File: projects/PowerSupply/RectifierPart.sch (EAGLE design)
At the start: 12 parts, among them X1 IN, X2 PRI, X3 SEC, X4 OUT

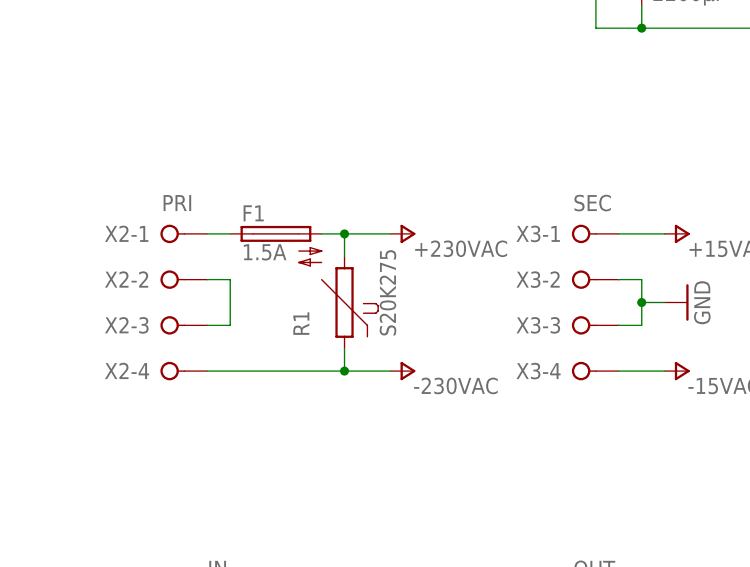
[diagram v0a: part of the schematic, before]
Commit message: fix(rect): replaced s20k275 with s20k230
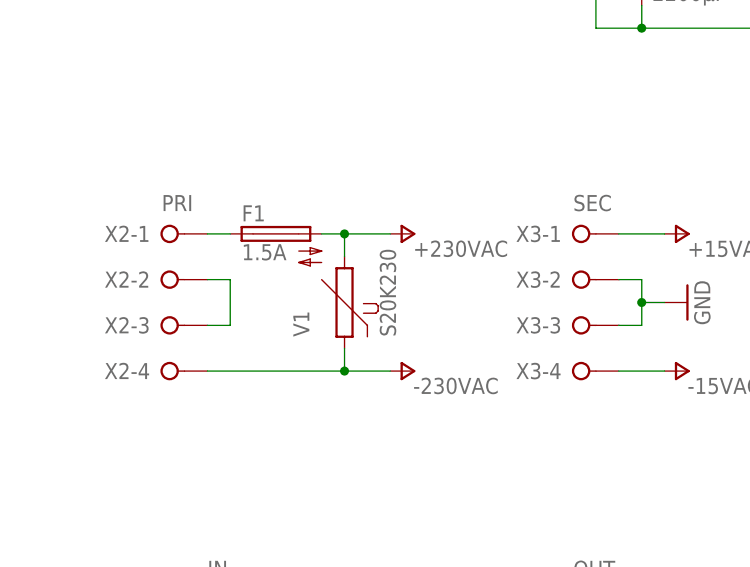
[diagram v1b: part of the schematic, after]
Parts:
- removed R1: S20K275, varistor:S20K275
- added V1: S20K230, varistor:S20K230
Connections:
- net +230VAC: now also V1.2; no longer R1.2
- net -230VAC: now also V1.1; no longer R1.1
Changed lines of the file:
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@@
 <grid distance="0.1" unitdist="inch" unit="inch" style="lines" multiple="1" display="no" altdistance="0.01" altunitdist="inch" altunit="inch"/>
 <layers>
-<layer number="1" name="Top" color="4" fill="1" visible="no" active="no"/>
-<layer number="16" name="Bottom" color="1" fill="1" visible="no" active="no"/>
-<layer number="17" name="Pads" color="2" fill="1" visible="no" active="no"/>
-<layer number="18" name="Vias" color="2" fill="1" visible="no" active="no"/>
-<layer number="19" name="Unrouted" color="6" fill="1" visible="no" active="no"/>
-<layer number="20" name="Dimension" color="24" fill="1" visible="no" active="no"/>
-<layer number="21" name="tPlace" color="7" fill="1" visible="no" active="no"/>
-<layer number="22" name="bPlace" color="7" fill="1" visible="no" active="no"/>
-<layer number="23" name="tOrigins" color="15" fill="1" visible="no" active="no"/>
-<layer number="24" name="bOrigins" color="15" fill="1" visible="no" active="no"/>
-<layer number="25" name="tNames" color="7" fill="1" visible="no" active="no"/>
-<layer number="26" name="bNames" color="7" fill="1" visible="no" active="no"/>
-<layer number="27" name="tValues" color="7" fill="1" visible="no" active="no"/>
-<layer number="28" name="bValues" color="7" fill="1" visible="no" active="no"/>
+<layer number="1" name="Top" color="4" fill="1" visible="yes" active="no"/>
+<layer number="16" name="Bottom" color="1" fill="1" visible="yes" active="no"/>
+<layer number="17" name="Pads" color="2" fill="1" visible="yes" active="no"/>
+<layer number="18" name="Vias" color="2" fill="1" visible="yes" active="no"/>
+<layer number="19" name="Unrouted" color="6" fill="1" visible="yes" active="no"/>
+<layer number="20" name="Dimension" color="24" fill="1" visible="yes" active="no"/>
+<layer number="21" name="tPlace" color="7" fill="1" visible="yes" active="no"/>
+<layer number="22" name="bPlace" color="7" fill="1" visible="yes" active="no"/>
+<layer number="23" name="tOrigins" color="15" fill="1" visible="yes" active="no"/>
+<layer number="24" name="bOrigins" color="15" fill="1" visible="yes" active="no"/>
+<layer number="25" name="tNames" color="7" fill="1" visible="yes" active="no"/>
+<layer number="26" name="bNames" color="7" fill="1" visible="yes" active="no"/>
+<layer number="27" name="tValues" color="7" fill="1" visible="yes" active="no"/>
+<layer number="28" name="bValues" color="7" fill="1" visible="yes" active="no"/>
 <layer number="29" name="tStop" color="7" fill="3" visible="no" active="no"/>
 <layer number="30" name="bStop" color="7" fill="6" visible="no" active="no"/>
@@
 <layer number="35" name="tGlue" color="7" fill="4" visible="no" active="no"/>
 <layer number="36" name="bGlue" color="7" fill="5" visible="no" active="no"/>
-<layer number="37" name="tTest" color="7" fill="1" visible="no" active="no"/>
-<layer number="38" name="bTest" color="7" fill="1" visible="no" active="no"/>
+<layer number="37" name="tTest" color="7" fill="1" visible="yes" active="no"/>
+<layer number="38" name="bTest" color="7" fill="1" visible="yes" active="no"/>
 <layer number="39" name="tKeepout" color="4" fill="11" visible="no" active="no"/>
 <layer number="40" name="bKeepout" color="1" fill="11" visible="no" active="no"/>
@@
 <layer number="44" name="Drills" color="7" fill="1" visible="no" active="no"/>
 <layer number="45" name="Holes" color="7" fill="1" visible="no" active="no"/>
-<layer number="46" name="Milling" color="3" fill="1" visible="no" active="no"/>
-<layer number="47" name="Measures" color="7" fill="1" visible="no" active="no"/>
-<layer number="48" name="Document" color="7" fill="1" visible="no" active="no"/>
-<layer number="49" name="Reference" color="7" fill="1" visible="no" active="no"/>
-<layer number="51" name="tDocu" color="7" fill="1" visible="no" active="no"/>
-<layer number="52" name="bDocu" color="7" fill="1" visible="no" active="no"/>
+<layer number="46" name="Milling" color="3" fill="1" visible="yes" active="no"/>
+<layer number="47" name="Measures" color="7" fill="1" visible="yes" active="no"/>
+<layer number="48" name="Document" color="7" fill="1" visible="yes" active="no"/>
+<layer number="49" name="Reference" color="7" fill="1" visible="yes" active="no"/>
+<layer number="51" name="tDocu" color="7" fill="1" visible="yes" active="no"/>
+<layer number="52" name="bDocu" color="7" fill="1" visible="yes" active="no"/>
 <layer number="88" name="SimResults" color="9" fill="1" visible="yes" active="yes"/>
 <layer number="89" name="SimProbes" color="9" fill="1" visible="yes" active="yes"/>
@@
 <part name="C4" library="rcl" library_urn="urn:adsk.eagle:library:334" deviceset="CPOL-EU" device="E7.5-16" package3d_urn="urn:adsk.eagle:package:23382/2" value="2200µF"/>
 <part name="FRAME1" library="frames" library_urn="urn:adsk.eagle:library:229" deviceset="A4L-LOC" device=""/>
-<part name="R1" library="varistor" library_urn="urn:adsk.eagle:library:410" deviceset="S20K275" device="" package3d_urn="urn:adsk.eagle:package:30604/1"/>
+<part name="V1" library="varistor" library_urn="urn:adsk.eagle:library:410" deviceset="S20K230" device="" package3d_urn="urn:adsk.eagle:package:30579/1"/>
 <part name="F1" library="fuse" library_urn="urn:adsk.eagle:library:233" deviceset="SH22,5A" device="" package3d_urn="urn:adsk.eagle:package:14070/1" value="1.5A"/>
 <part name="F2" library="fuse" library_urn="urn:adsk.eagle:library:233" deviceset="SH22,5A" device="" package3d_urn="urn:adsk.eagle:package:14070/1" value="10A"/>
@@
 <attribute name="SHEET" x="230.505" y="5.08" size="2.54" layer="94"/>
 </instance>
-<instance part="R1" gate="G$1" x="45.72" y="109.22" smashed="yes" rot="R90">
+<instance part="V1" gate="G$1" x="45.72" y="109.22" smashed="yes" rot="R90">
 <attribute name="NAME" x="41.8084" y="105.41" size="1.778" layer="95" rot="R90"/>
 <attribute name="VALUE" x="51.435" y="105.41" size="1.778" layer="96" rot="R90"/>
@@
 <pinref part="F1" gate="1" pin="2"/>
 <wire x1="43.18" y1="116.84" x2="45.72" y2="116.84" width="0.1524" layer="91"/>
-<pinref part="R1" gate="G$1" pin="2"/>
+<pinref part="V1" gate="G$1" pin="2"/>
 <wire x1="45.72" y1="116.84" x2="50.8" y2="116.84" width="0.1524" layer="91"/>
 <wire x1="45.72" y1="114.3" x2="45.72" y2="116.84" width="0.1524" layer="91"/>
@@
 <pinref part="X2" gate="-4" pin="KL"/>
 <wire x1="50.8" y1="101.6" x2="45.72" y2="101.6" width="0.1524" layer="91"/>
-<pinref part="R1" gate="G$1" pin="1"/>
+<pinref part="V1" gate="G$1" pin="1"/>
 <wire x1="45.72" y1="101.6" x2="30.48" y2="101.6" width="0.1524" layer="91"/>
 <wire x1="45.72" y1="104.14" x2="45.72" y2="101.6" width="0.1524" layer="91"/>

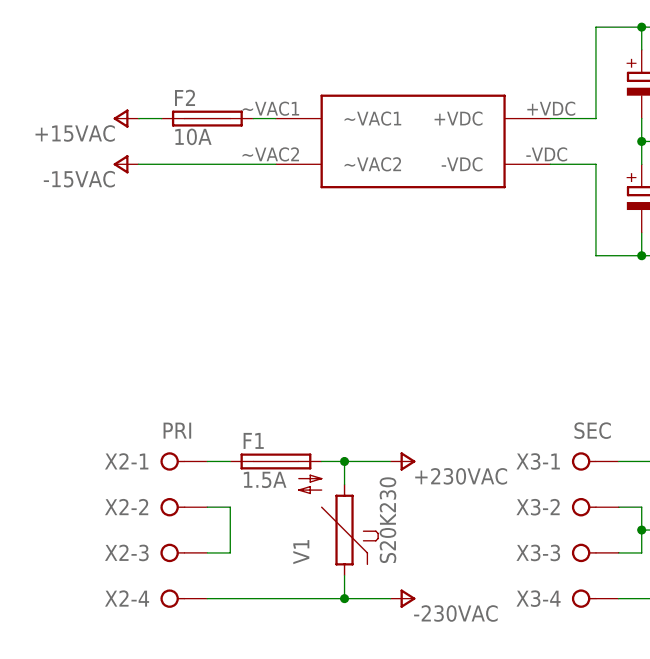
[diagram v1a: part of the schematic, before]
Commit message: feat: rectifier fuse values modified
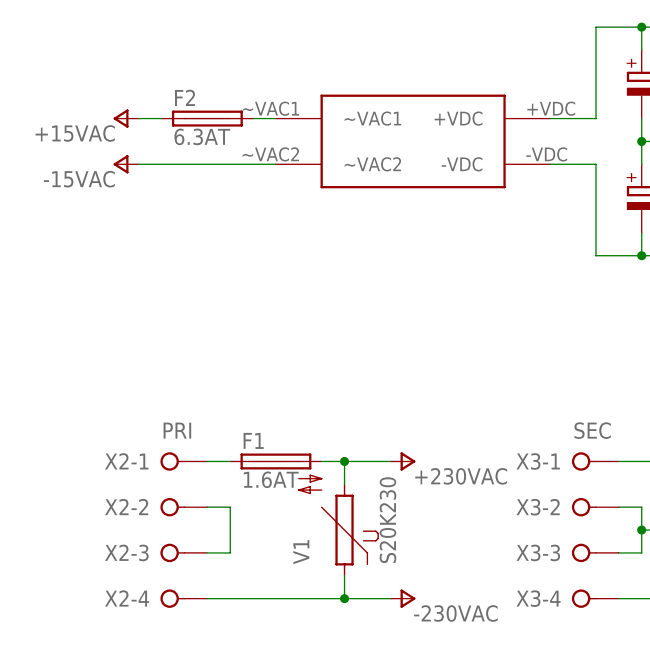
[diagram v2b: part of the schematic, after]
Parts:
- F1: value 1.5A -> 1.6AT
- F2: value 10A -> 6.3AT
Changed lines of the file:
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@@
 <grid distance="0.1" unitdist="inch" unit="inch" style="lines" multiple="1" display="no" altdistance="0.01" altunitdist="inch" altunit="inch"/>
 <layers>
-<layer number="1" name="Top" color="4" fill="1" visible="yes" active="no"/>
-<layer number="16" name="Bottom" color="1" fill="1" visible="yes" active="no"/>
-<layer number="17" name="Pads" color="2" fill="1" visible="yes" active="no"/>
-<layer number="18" name="Vias" color="2" fill="1" visible="yes" active="no"/>
-<layer number="19" name="Unrouted" color="6" fill="1" visible="yes" active="no"/>
-<layer number="20" name="Dimension" color="24" fill="1" visible="yes" active="no"/>
-<layer number="21" name="tPlace" color="7" fill="1" visible="yes" active="no"/>
-<layer number="22" name="bPlace" color="7" fill="1" visible="yes" active="no"/>
-<layer number="23" name="tOrigins" color="15" fill="1" visible="yes" active="no"/>
-<layer number="24" name="bOrigins" color="15" fill="1" visible="yes" active="no"/>
-<layer number="25" name="tNames" color="7" fill="1" visible="yes" active="no"/>
-<layer number="26" name="bNames" color="7" fill="1" visible="yes" active="no"/>
-<layer number="27" name="tValues" color="7" fill="1" visible="yes" active="no"/>
-<layer number="28" name="bValues" color="7" fill="1" visible="yes" active="no"/>
+<layer number="1" name="Top" color="4" fill="1" visible="no" active="no"/>
+<layer number="16" name="Bottom" color="1" fill="1" visible="no" active="no"/>
+<layer number="17" name="Pads" color="2" fill="1" visible="no" active="no"/>
+<layer number="18" name="Vias" color="2" fill="1" visible="no" active="no"/>
+<layer number="19" name="Unrouted" color="6" fill="1" visible="no" active="no"/>
+<layer number="20" name="Dimension" color="24" fill="1" visible="no" active="no"/>
+<layer number="21" name="tPlace" color="7" fill="1" visible="no" active="no"/>
+<layer number="22" name="bPlace" color="7" fill="1" visible="no" active="no"/>
+<layer number="23" name="tOrigins" color="15" fill="1" visible="no" active="no"/>
+<layer number="24" name="bOrigins" color="15" fill="1" visible="no" active="no"/>
+<layer number="25" name="tNames" color="7" fill="1" visible="no" active="no"/>
+<layer number="26" name="bNames" color="7" fill="1" visible="no" active="no"/>
+<layer number="27" name="tValues" color="7" fill="1" visible="no" active="no"/>
+<layer number="28" name="bValues" color="7" fill="1" visible="no" active="no"/>
 <layer number="29" name="tStop" color="7" fill="3" visible="no" active="no"/>
 <layer number="30" name="bStop" color="7" fill="6" visible="no" active="no"/>
@@
 <layer number="35" name="tGlue" color="7" fill="4" visible="no" active="no"/>
 <layer number="36" name="bGlue" color="7" fill="5" visible="no" active="no"/>
-<layer number="37" name="tTest" color="7" fill="1" visible="yes" active="no"/>
-<layer number="38" name="bTest" color="7" fill="1" visible="yes" active="no"/>
+<layer number="37" name="tTest" color="7" fill="1" visible="no" active="no"/>
+<layer number="38" name="bTest" color="7" fill="1" visible="no" active="no"/>
 <layer number="39" name="tKeepout" color="4" fill="11" visible="no" active="no"/>
 <layer number="40" name="bKeepout" color="1" fill="11" visible="no" active="no"/>
@@
 <layer number="44" name="Drills" color="7" fill="1" visible="no" active="no"/>
 <layer number="45" name="Holes" color="7" fill="1" visible="no" active="no"/>
-<layer number="46" name="Milling" color="3" fill="1" visible="yes" active="no"/>
-<layer number="47" name="Measures" color="7" fill="1" visible="yes" active="no"/>
-<layer number="48" name="Document" color="7" fill="1" visible="yes" active="no"/>
-<layer number="49" name="Reference" color="7" fill="1" visible="yes" active="no"/>
-<layer number="51" name="tDocu" color="7" fill="1" visible="yes" active="no"/>
-<layer number="52" name="bDocu" color="7" fill="1" visible="yes" active="no"/>
+<layer number="46" name="Milling" color="3" fill="1" visible="no" active="no"/>
+<layer number="47" name="Measures" color="7" fill="1" visible="no" active="no"/>
+<layer number="48" name="Document" color="7" fill="1" visible="no" active="no"/>
+<layer number="49" name="Reference" color="7" fill="1" visible="no" active="no"/>
+<layer number="51" name="tDocu" color="7" fill="1" visible="no" active="no"/>
+<layer number="52" name="bDocu" color="7" fill="1" visible="no" active="no"/>
 <layer number="88" name="SimResults" color="9" fill="1" visible="yes" active="yes"/>
 <layer number="89" name="SimProbes" color="9" fill="1" visible="yes" active="yes"/>
@@
 <part name="FRAME1" library="frames" library_urn="urn:adsk.eagle:library:229" deviceset="A4L-LOC" device=""/>
 <part name="V1" library="varistor" library_urn="urn:adsk.eagle:library:410" deviceset="S20K230" device="" package3d_urn="urn:adsk.eagle:package:30579/1"/>
-<part name="F1" library="fuse" library_urn="urn:adsk.eagle:library:233" deviceset="SH22,5A" device="" package3d_urn="urn:adsk.eagle:package:14070/1" value="1.5A"/>
-<part name="F2" library="fuse" library_urn="urn:adsk.eagle:library:233" deviceset="SH22,5A" device="" package3d_urn="urn:adsk.eagle:package:14070/1" value="10A"/>
+<part name="F1" library="fuse" library_urn="urn:adsk.eagle:library:233" deviceset="SH22,5A" device="" package3d_urn="urn:adsk.eagle:package:14070/1" value="1.6AT"/>
+<part name="F2" library="fuse" library_urn="urn:adsk.eagle:library:233" deviceset="SH22,5A" device="" package3d_urn="urn:adsk.eagle:package:14070/1" value="6.3AT"/>
 <part name="X1" library="con-wago-508" library_urn="urn:adsk.eagle:library:196" deviceset="W237-03P" device="" package3d_urn="urn:adsk.eagle:package:10737/1" value="IN"/>
 <part name="PE1" library="supply1" library_urn="urn:adsk.eagle:library:371" deviceset="PE" device=""/>
